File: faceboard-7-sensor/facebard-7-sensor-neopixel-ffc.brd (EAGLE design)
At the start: 26 x 93.5 mm, 32 parts, among them Q1 QRE1113, Q2 QRE1113, Q3 QRE1113, Q4 QRE1113, Q5 QRE1113, Q6 QRE1113, Q7 QRE1113, U1 CD4051BE

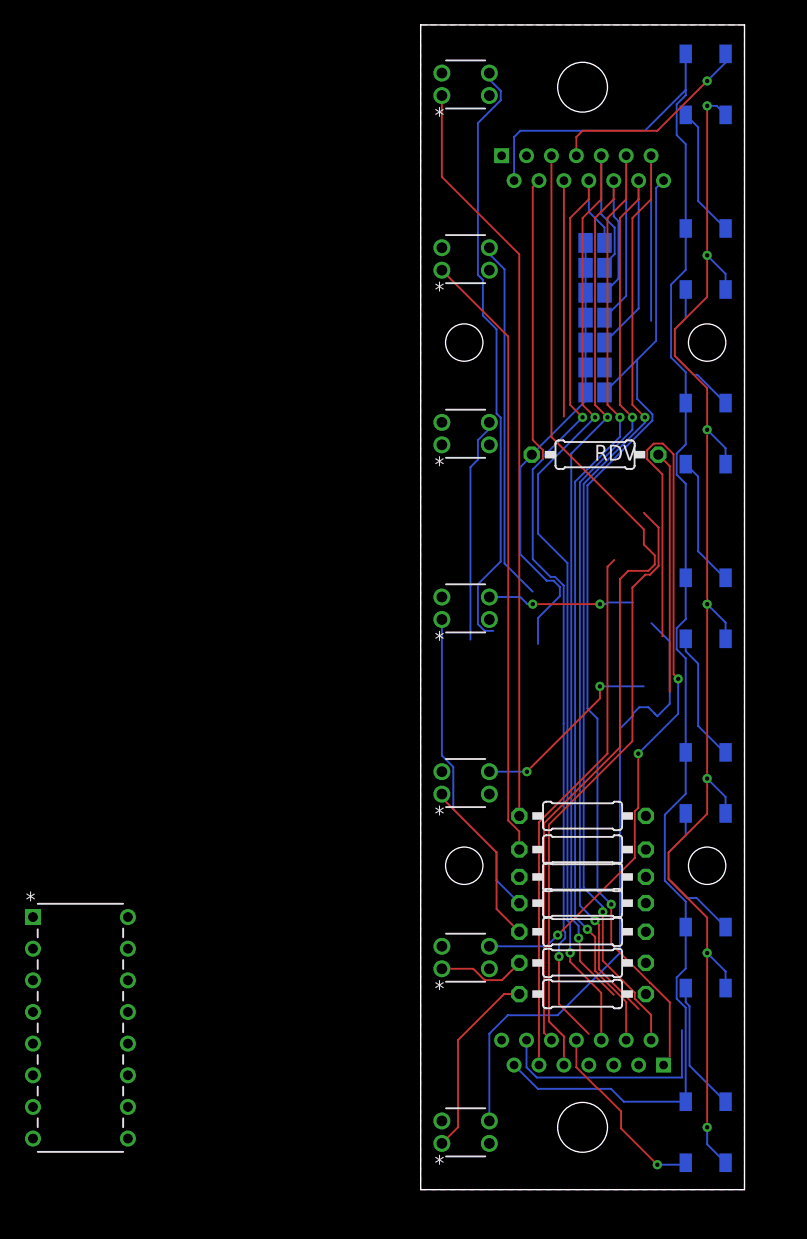
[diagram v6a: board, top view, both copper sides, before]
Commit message: rewire mini leds and dividing resistors
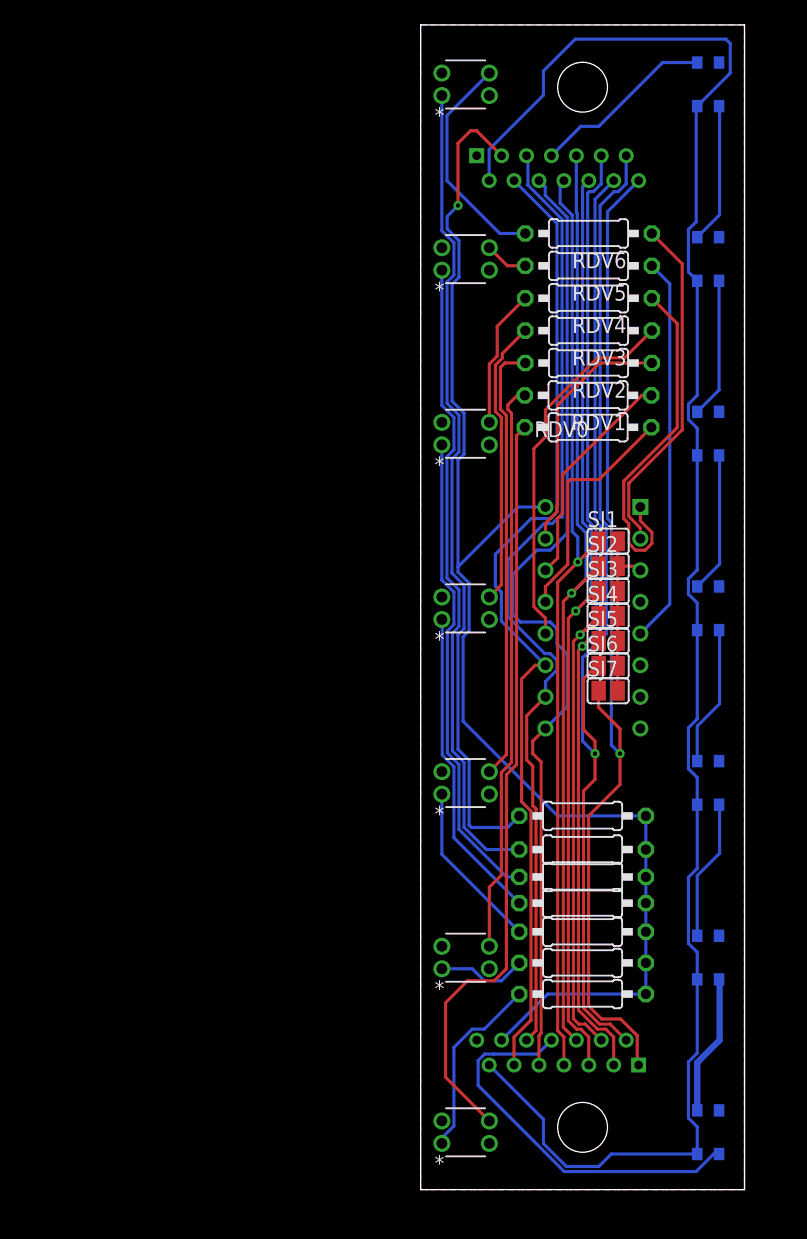
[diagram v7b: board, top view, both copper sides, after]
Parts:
- removed D1, D2, D3, D4, D5, D6, D7: 1655, 1655:LED_1655
- removed RDV: 100k, rcl:0207/10
- added LED1, LED2, LED3, LED4, LED5, LED6, LED7: WS2812B3535, adafruit:LED3535
- added RDV0, RDV1, RDV2, RDV3, RDV4, RDV5, RDV6: 100k, rcl:0207/10
- moved U1 58.8 mm to (17.6, 54.8), flipped to the bottom
- moved SJ1 24.0 mm to (15.1, 52.0), flipped to the top
- moved SJ2 24.0 mm to (15.1, 50.0), flipped to the top
- moved SJ3 24.0 mm to (15.1, 48.0), flipped to the top
- moved SJ4 24.0 mm to (15.1, 46.0), flipped to the top
- moved SJ5 24.0 mm to (15.1, 44.0), flipped to the top
- moved SJ6 24.0 mm to (15.1, 42.0), flipped to the top
- moved SJ7 24.0 mm to (15.1, 40.0), flipped to the top
- moved FFCIN 2.00 mm to (17.5, 10.0)
- moved FFCOUT 2.00 mm to (4.50, 83.0)
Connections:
- removed net N$15: D6.4, D7.2
- removed net N$16: D1.4, D2.2
- removed net N$17: D2.4, D3.2
- removed net N$18: D3.4, D4.2
- removed net N$19: D4.4, D5.2
- removed net N$2: FFCOUT.3, R1.1, R11.1, R13.1, R3.1, R5.1, R7.1, R9.1
- removed net N$20: D5.4, D6.2
- removed net VCC: FFCIN.12, RDV.2, U1.16
- new net 5V: FFCIN.12, FFCOUT.3, R1.1, R11.1, R13.1, R3.1, R5.1, R7.1, R9.1, U1.16
- new net N$10: LED5.3, LED6.1
- new net N$12: LED6.3, LED7.1
- new net N$14: Q5.1, R9.2
- new net N$4: LED1.3, LED2.1
- new net N$6: LED2.3, LED3.1
- new net N$8: LED3.3, LED4.1
- new net N$9: LED4.3, LED5.1
- new net RDV0: Q1.3, RDV0.2
- new net RDV1: Q2.3, RDV1.2
- new net RDV2: Q3.3, RDV2.2
- new net RDV3: Q4.3, RDV3.2
- new net RDV4: Q5.3, RDV4.2
- new net RDV5: Q6.3, RDV5.2
- new net RDV6: Q7.3, RDV6.2
- net 3V: now also LED1.2, LED2.2, LED3.2, LED4.2, LED5.2, LED6.2, LED7.2; no longer D1.3, D2.3, D3.3, D4.3, D5.3, D6.3, D7.3
- net C0: now also RDV0.1; no longer Q1.3
- net C1: now also RDV1.1; no longer Q2.3
- net C2: now also RDV2.1; no longer Q3.3
- net C3: now also RDV3.1; no longer Q4.3
- net C4: now also RDV4.1; no longer Q5.3
- net C5: now also RDV5.1; no longer Q6.3
- net C6: now also RDV6.1; no longer Q7.3
- net DIN: now also LED1.1; no longer D1.2
- net DOUT: now also LED7.3; no longer D7.4
- net GND: now also FFCIN.14, LED1.4, LED2.4, LED3.4, LED4.4, LED5.4, LED6.4, LED7.4; no longer D1.1, D2.1, D3.1, D4.1, D5.1, D6.1, D7.1
- net SIG: no longer RDV.1
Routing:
- net GND: track 108.9 -> 0.00 mm, vias 7 -> 0
- net 5V: track 0.00 -> 107.5 mm, vias 0 -> 1
- net RDV0: track 0.00 -> 61.0 mm
- net C1: track 66.8 -> 18.0 mm, vias 3 -> 0
- net RDV1: track 0.00 -> 46.0 mm
- net N$14: track 0.00 -> 38.3 mm
- net VCC: track 38.2 -> 0.00 mm
- net RDV2: track 0.00 -> 35.4 mm
- net C0: track 50.8 -> 18.9 mm
- net RDV3: track 0.00 -> 23.0 mm
- net SIG: track 36.0 -> 14.0 mm
- net C6: track 48.3 -> 27.7 mm
- net 3V: track 122.7 -> 142.2 mm
- net RDV6: track 0.00 -> 18.1 mm
- net C3: track 11.8 -> 29.9 mm, vias 2 -> 0
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
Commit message: fix signal routing
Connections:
- removed net RDV0: Q1.3, RDV0.2
- removed net RDV1: Q2.3, RDV1.2
- removed net RDV2: Q3.3, RDV2.2
- removed net RDV3: Q4.3, RDV3.2
- removed net RDV4: Q5.3, RDV4.2
- removed net RDV5: Q6.3, RDV5.2
- removed net RDV6: Q7.3, RDV6.2
- net 5V: now also RDV0.1, RDV1.1, RDV2.1, RDV3.1, RDV4.1, RDV5.1, RDV6.1
- net C0: now also Q1.3, RDV0.2; no longer RDV0.1
- net C1: now also Q2.3, RDV1.2; no longer RDV1.1
- net C2: now also Q3.3, RDV2.2; no longer RDV2.1
- net C3: now also Q4.3, RDV3.2; no longer RDV3.1
- net C4: now also Q5.3, RDV4.2; no longer RDV4.1
- net C5: now also Q6.3, RDV5.2; no longer RDV5.1
- net C6: now also Q7.3, RDV6.2; no longer RDV6.1
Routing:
- net RDV0: track 61.0 -> 0.00 mm
- net C0: track 18.9 -> 65.8 mm, vias 0 -> 1
- net RDV1: track 46.0 -> 0.00 mm
- net C1: track 18.0 -> 62.3 mm
- net 5V: track 107.5 -> 143.3 mm
- net RDV2: track 35.4 -> 0.00 mm
- net C2: track 20.1 -> 52.3 mm
- net RDV3: track 23.0 -> 0.00 mm
- net C6: track 27.7 -> 50.5 mm
- net C3: track 29.9 -> 52.2 mm
- net RDV6: track 18.1 -> 0.00 mm
- net RDV4: track 11.2 -> 0.00 mm
- net C5: track 31.1 -> 41.5 mm
- net C4: track 28.1 -> 31.7 mm
- net RDV5: track 3.49 -> 0.00 mm
